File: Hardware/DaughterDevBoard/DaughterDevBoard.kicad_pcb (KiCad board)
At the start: 2 copper layers, 145 x 160 mm, 64 parts, among them J1 PS/2, J10 I/O_PWR, J11 DIVIDER, J12 AUDIO_OUT, J13 BANKA, J14 BANKB, J15 BANKD, J16 BANKC, J17 VGA_OUT, J18 SD_CARD, J2 I/O0, J3 ISA1, J4 ISA0, J5 I/O1, J6 CPU_CLOCK, J7 JOYPAD1, J9 LCD, U1 74HC590A, U2 ATmega328P-PU, U3 SN74LVC2T45QDCURQ1, U4 SN74LVC2T45QDCURQ1, U5 SN74LVC2T45QDCURQ1, U6 SN74LVC8T245DBQR, U7 SN74LVC8T245DBQR, U8 SN74LVC8T245DBQR, X1 ACO-20MHz

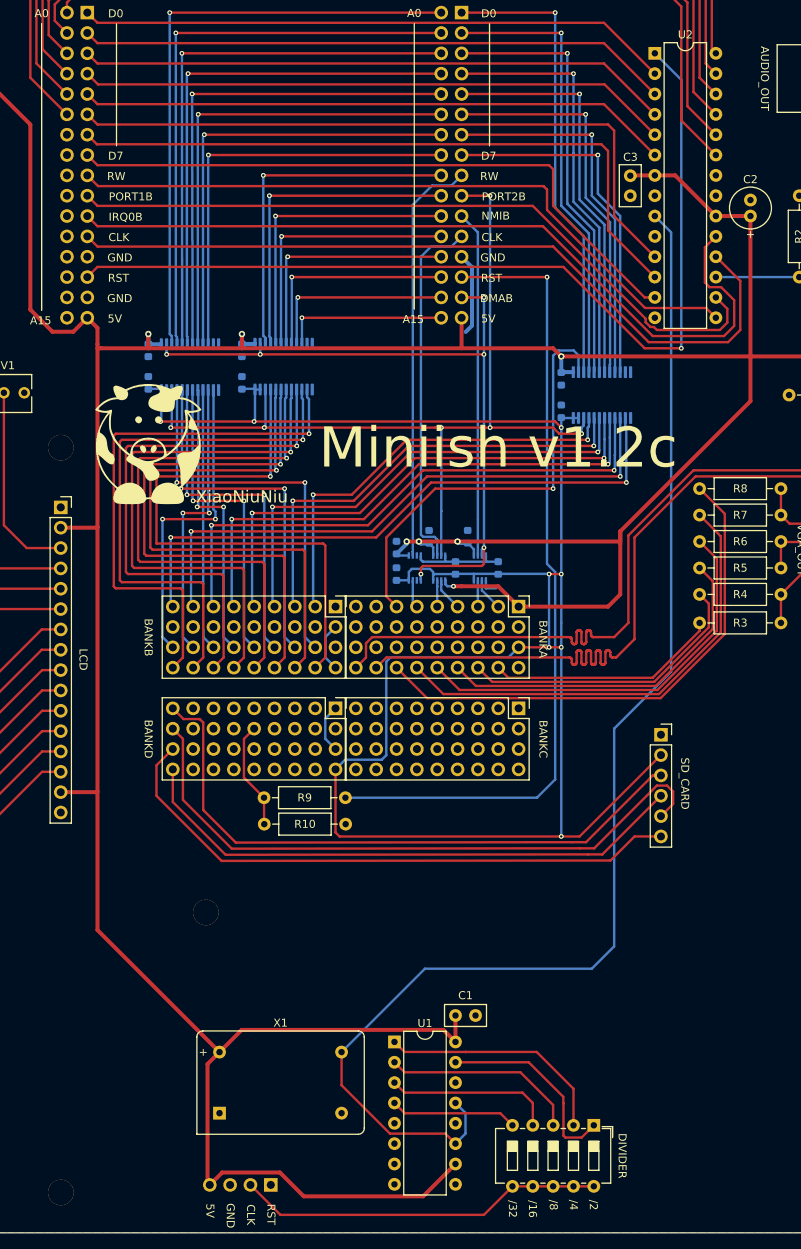
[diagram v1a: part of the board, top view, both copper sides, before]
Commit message: Fix Reset, WAI Signal, Add PROG jumper and reformat luc files
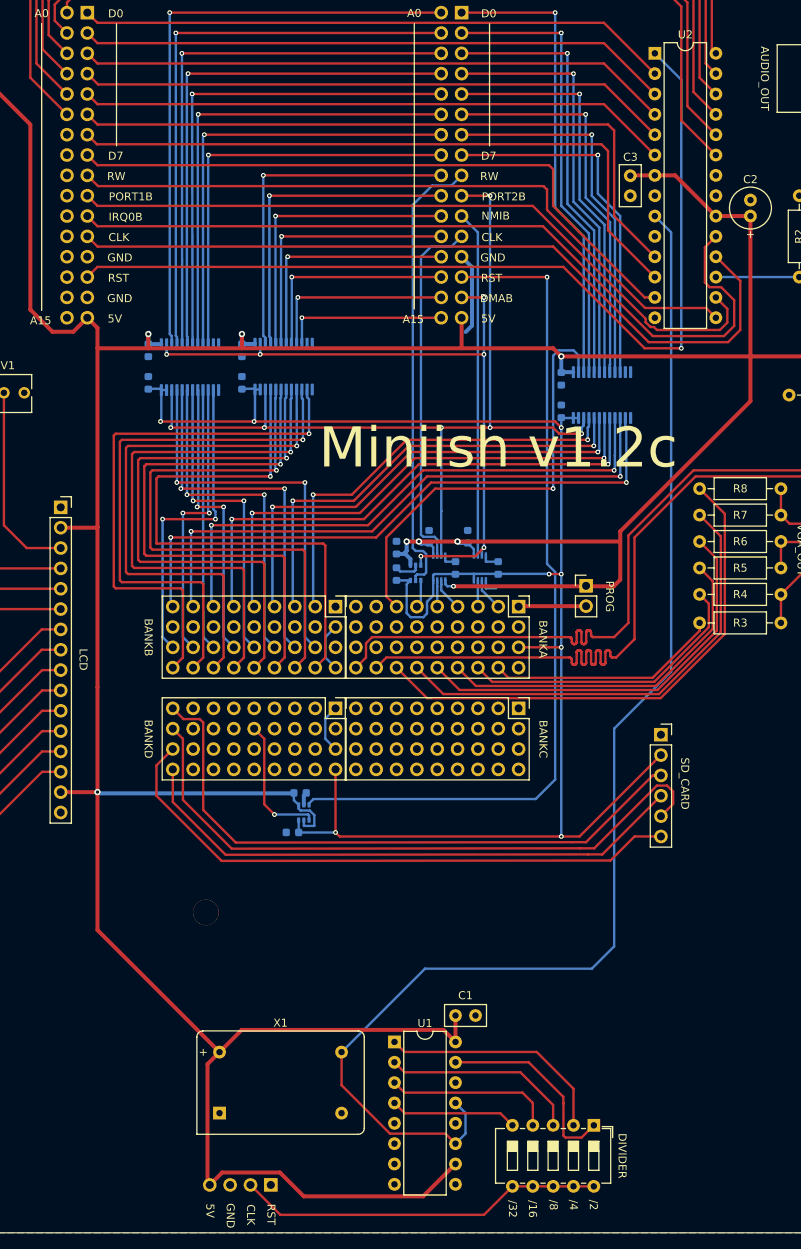
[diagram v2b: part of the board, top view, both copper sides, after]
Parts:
- removed R10: 3K3, Resistor_THT:R_Axial_DIN0207_L6.3mm_D2.5mm_P10.16mm_Horizontal
- removed R9: 2K2, Resistor_THT:R_Axial_DIN0207_L6.3mm_D2.5mm_P10.16mm_Horizontal
- removed REF** (x2): MountingHole_3.2mm_M3, MountingHole:MountingHole_3.2mm_M3
- removed XiaoNiuNiu: LOGO, Logos:SmallCow
- added C18: 100nF, Capacitor_SMD:C_0603_1608Metric, B.Cu at (92.4, 130.5)
- added C19: 100nF, Capacitor_SMD:C_0603_1608Metric, B.Cu at (91.4, 135.4)
- added J8: PROG, Connector_PinHeader_2.54mm:PinHeader_1x02_P2.54mm_Vertical, F.Cu at (128.1, 104.6)
- added U9: SN74LVC1T45DCK, Package_TO_SOT_SMD:SOT-363_SC-70-6, B.Cu at (106.8, 103.0)
- R3, R5, R7: value 1K -> 1.5K
- R4, R6, R8: value 470 -> 680
- U5: value SN74LVC2T45QDCURQ1 -> SN74LVC1T45DCK; footprint Package_SO:VSSOP-8_2.3x2mm_P0.5mm -> Package_TO_SOT_SMD:SOT-363_SC-70-6
- moved U5 33.5 mm to (92.8, 132.9)
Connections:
- net /CLOCK1 renamed /VGA Card/CLOCK1
- net /CLOCK1_1 renamed /SoundCard/CLOCK1
- net /CSB renamed /SoundCard/CSB
- net /CSB_1 renamed /VGA Card/CSB
- net /IRQB renamed /SoundCard/IRQB
- net /NMIB renamed /VGA Card/NMIB
- net /RESET renamed /SoundCard/RESET
- net /RW renamed /SoundCard/RW
- J1 pad 2: (no net) -> unconnected-(J1-Pad2)
- J1 pad 6: (no net) -> unconnected-(J1-Pad6)
- J13 pad 1: +5V -> Net-(J13-Pad1)
- J13 pad 11: (no net) -> unconnected-(J13-Pad11)
- J13 pad 12: (no net) -> unconnected-(J13-Pad12)
- J13 pad 13: (no net) -> unconnected-(J13-Pad13)
- J13 pad 14: (no net) -> unconnected-(J13-Pad14)
- J13 pad 15: (no net) -> unconnected-(J13-Pad15)
- J13 pad 16: (no net) -> unconnected-(J13-Pad16)
- J13 pad 17: (no net) -> unconnected-(J13-Pad17)
- J13 pad 18: (no net) -> unconnected-(J13-Pad18)
- J13 pad 19: (no net) -> unconnected-(J13-Pad19)
- J13 pad 20: (no net) -> unconnected-(J13-Pad20)
- J13 pad 21: (no net) -> unconnected-(J13-Pad21)
- J13 pad 22: (no net) -> unconnected-(J13-Pad22)
- J13 pad 23: (no net) -> unconnected-(J13-Pad23)
- J13 pad 24: (no net) -> unconnected-(J13-Pad24)
- J13 pad 25: (no net) -> unconnected-(J13-Pad25)
- J13 pad 26: (no net) -> unconnected-(J13-Pad26)
- J13 pad 8: (no net) -> unconnected-(J13-Pad8)
- J13 pad 9: (no net) -> unconnected-(J13-Pad9)
- J14 pad 1: (no net) -> unconnected-(J14-Pad1)
- J14 pad 11: (no net) -> unconnected-(J14-Pad11)
- J14 pad 12: (no net) -> unconnected-(J14-Pad12)
- J14 pad 13: (no net) -> unconnected-(J14-Pad13)
- J14 pad 14: (no net) -> unconnected-(J14-Pad14)
- J14 pad 15: (no net) -> unconnected-(J14-Pad15)
- J14 pad 16: (no net) -> unconnected-(J14-Pad16)
- J14 pad 17: (no net) -> unconnected-(J14-Pad17)
- J14 pad 18: (no net) -> unconnected-(J14-Pad18)
- J14 pad 27: (no net) -> unconnected-(J14-Pad27)
- J15 pad 10: (no net) -> unconnected-(J15-Pad10)
- J15 pad 11: (no net) -> unconnected-(J15-Pad11)
- J15 pad 12: (no net) -> unconnected-(J15-Pad12)
- J15 pad 13: (no net) -> unconnected-(J15-Pad13)
- J15 pad 15: (no net) -> unconnected-(J15-Pad15)
- J15 pad 16: (no net) -> unconnected-(J15-Pad16)
- J15 pad 17: (no net) -> unconnected-(J15-Pad17)
- J15 pad 2: (no net) -> unconnected-(J15-Pad2)
- J15 pad 20: (no net) -> unconnected-(J15-Pad20)
- J15 pad 21: (no net) -> unconnected-(J15-Pad21)
- J15 pad 22: (no net) -> unconnected-(J15-Pad22)
- J15 pad 23: (no net) -> unconnected-(J15-Pad23)
- J15 pad 24: (no net) -> unconnected-(J15-Pad24)
- J15 pad 25: (no net) -> unconnected-(J15-Pad25)
- J15 pad 26: (no net) -> unconnected-(J15-Pad26)
- J15 pad 29: (no net) -> unconnected-(J15-Pad29)
- J15 pad 3: (no net) -> unconnected-(J15-Pad3)
- J15 pad 30: (no net) -> unconnected-(J15-Pad30)
- J15 pad 31: (no net) -> unconnected-(J15-Pad31)
- J15 pad 32: (no net) -> unconnected-(J15-Pad32)
- J15 pad 33: (no net) -> unconnected-(J15-Pad33)
- J15 pad 34: (no net) -> unconnected-(J15-Pad34)
- J15 pad 35: (no net) -> unconnected-(J15-Pad35)
- J15 pad 4: (no net) -> unconnected-(J15-Pad4)
- J15 pad 5: (no net) -> unconnected-(J15-Pad5)
- J15 pad 6: (no net) -> unconnected-(J15-Pad6)
- J15 pad 7: (no net) -> unconnected-(J15-Pad7)
- J15 pad 8: (no net) -> unconnected-(J15-Pad8)
- J16 pad 10: (no net) -> unconnected-(J16-Pad10)
- J16 pad 11: (no net) -> unconnected-(J16-Pad11)
- J16 pad 12: (no net) -> unconnected-(J16-Pad12)
- J16 pad 13: (no net) -> unconnected-(J16-Pad13)
- J16 pad 14: (no net) -> unconnected-(J16-Pad14)
- J16 pad 15: (no net) -> unconnected-(J16-Pad15)
- J16 pad 16: (no net) -> unconnected-(J16-Pad16)
- J16 pad 17: (no net) -> unconnected-(J16-Pad17)
- J16 pad 18: (no net) -> unconnected-(J16-Pad18)
- J16 pad 19: (no net) -> unconnected-(J16-Pad19)
- J16 pad 2: (no net) -> unconnected-(J16-Pad2)
- J16 pad 20: (no net) -> unconnected-(J16-Pad20)
- J16 pad 21: (no net) -> unconnected-(J16-Pad21)
- J16 pad 22: (no net) -> unconnected-(J16-Pad22)
- J16 pad 23: (no net) -> unconnected-(J16-Pad23)
- J16 pad 24: (no net) -> unconnected-(J16-Pad24)
- J16 pad 25: (no net) -> unconnected-(J16-Pad25)
- J16 pad 26: (no net) -> unconnected-(J16-Pad26)
- J16 pad 28: (no net) -> unconnected-(J16-Pad28)
- J16 pad 29: (no net) -> unconnected-(J16-Pad29)
- J16 pad 3: (no net) -> unconnected-(J16-Pad3)
- J16 pad 30: (no net) -> unconnected-(J16-Pad30)
- J16 pad 31: (no net) -> unconnected-(J16-Pad31)
- J16 pad 32: (no net) -> unconnected-(J16-Pad32)
- J16 pad 33: (no net) -> unconnected-(J16-Pad33)
- J16 pad 34: (no net) -> unconnected-(J16-Pad34)
- J16 pad 35: (no net) -> unconnected-(J16-Pad35)
- J16 pad 36: (no net) -> unconnected-(J16-Pad36)
- J16 pad 4: (no net) -> unconnected-(J16-Pad4)
- J16 pad 5: (no net) -> unconnected-(J16-Pad5)
- J16 pad 6: (no net) -> unconnected-(J16-Pad6)
- J16 pad 7: (no net) -> unconnected-(J16-Pad7)
- J16 pad 8: (no net) -> unconnected-(J16-Pad8)
- J16 pad 9: (no net) -> unconnected-(J16-Pad9)
- J17 pad 11: (no net) -> unconnected-(J17-Pad11)
- J17 pad 12: (no net) -> unconnected-(J17-Pad12)
- J17 pad 15: (no net) -> unconnected-(J17-Pad15)
- J17 pad 4: (no net) -> unconnected-(J17-Pad4)
- J17 pad 9: (no net) -> unconnected-(J17-Pad9)
- J2 pad 10: (no net) -> CA2
- J2 pad 9: (no net) -> CA1
- J3 pad 14: /RESET_1 -> /VGA Card/RESET
- J3 pad 15: /DMAB -> /VGA Card/DMAB
- J3 pad 9: /RW_1 -> /VGA Card/RW
- J4 pad 23: (no net) -> /AA6
- J4 pad 24: (no net) -> /AA7
- J4 pad 25: (no net) -> /AA8
- J4 pad 26: (no net) -> /AA9
- J4 pad 27: (no net) -> /AA10
- J4 pad 28: (no net) -> /AA11
- J4 pad 29: (no net) -> /AA12
- J4 pad 30: (no net) -> /AA13
- J4 pad 31: (no net) -> /AA14
- J4 pad 32: (no net) -> /AA15
- J5 pad 10: (no net) -> CB2
- J5 pad 9: (no net) -> CB1
- J6 pad 1: (no net) -> RESET
- J7 pad 5: (no net) -> unconnected-(J7-Pad5)
- J7 pad 6: (no net) -> unconnected-(J7-Pad6)
- RV1 pad 3: (no net) -> unconnected-(RV1-Pad3)
- U1 pad 5: (no net) -> unconnected-(U1-Pad5)
- U1 pad 6: (no net) -> unconnected-(U1-Pad6)
- U1 pad 7: (no net) -> unconnected-(U1-Pad7)
- U1 pad 9: (no net) -> unconnected-(U1-Pad9)
- U2 pad 10: (no net) -> unconnected-(U2-Pad10)
- U2 pad 14: (no net) -> unconnected-(U2-Pad14)
- U3 pad 3: /DMAB -> /VGA Card/DMAB
- U5 pad 2: /RW_1 -> GND
- U5 pad 3: (no net) -> /VGA Card/RESET
- U5 pad 4: GND -> Net-(J15-Pad14)
- U5 pad 5: /DMAB -> +5V
- U5 pad 6: (no net) -> +3V3
- U7 pad 2: /DMAB -> /VGA Card/DMAB
- U8 pad 2: /DMAB -> /VGA Card/DMAB
- X1 pad 1: (no net) -> unconnected-(X1-Pad1)
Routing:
- net /VGA Card/RESET: track 0.00 -> 106.0 mm, vias 0 -> 1
- net /RESET_1: track 101.0 -> 0.00 mm, vias 1 -> 0
- net /DMAB: track 89.0 -> 0.00 mm, vias 6 -> 0
- net /VGA Card/DMAB: track 0.00 -> 86.8 mm, vias 0 -> 6
- net /VGA Card/RW: track 0.00 -> 56.8 mm
- net /RW_1: track 51.4 -> 0.00 mm
- net +3V3: track 244.5 -> 212.3 mm
- net +5V: track 565.7 -> 594.3 mm, vias 7 -> 8
- net Net-(J13-Pad1): track 0.00 -> 8.53 mm
- net Net-(J15-Pad14): track 13.5 -> 16.7 mm, vias 0 -> 1
- net GND: track 43.9 -> 41.3 mm

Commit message: Cleanup and update version
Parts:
- added XiaoNiuNiu: LOGO, Logos:SmallCow, F.Cu at (42.0, 175.5)
- moved C18 2.87 mm to (89.9, 131.9), turned to 180 degrees
- moved C19 2.16 mm to (89.9, 133.9)
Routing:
- net +3V3: track 212.3 -> 213.4 mm
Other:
- board text added: "Miniish v1.2d"
- board text removed: "Miniish v1.2c"

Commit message: Cleanup
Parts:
- added C20: 100uF, Capacitor_THT:CP_Radial_D5.0mm_P2.50mm, F.Cu at (109.6, 146.9)
- added Q1: 2N2222A, Package_TO_SOT_THT:TO-18-3, F.Cu at (126.1, 157.7)
- added R10: 1K, Resistor_THT:R_Axial_DIN0207_L6.3mm_D2.5mm_P10.16mm_Horizontal, F.Cu at (114.7, 151.9)
- added R11: 10K, Resistor_THT:R_Axial_DIN0207_L6.3mm_D2.5mm_P10.16mm_Horizontal, F.Cu at (114.8, 144.3)
- added R9: 2.2K, Resistor_THT:R_Axial_DIN0207_L6.3mm_D2.5mm_P10.16mm_Horizontal, F.Cu at (114.8, 148.2)
- C18: value 100nF -> 100uF; footprint Capacitor_SMD:C_0603_1608Metric -> Capacitor_THT:CP_Radial_D5.0mm_P2.50mm; moved to F.Cu
- C19: value 100nF -> 10nF; footprint Capacitor_SMD:C_0603_1608Metric -> Capacitor_THT:C_Disc_D5.0mm_W2.5mm_P2.50mm; moved to F.Cu
- U5: value SN74LVC1T45DCK -> NE555P; footprint Package_TO_SOT_SMD:SOT-363_SC-70-6 -> Package_DIP:DIP-8_W7.62mm; moved to F.Cu
- moved J18 28.9 mm to (166.3, 123.0)
- moved C19 24.1 mm to (106.2, 151.6), turned to -90 degrees
- moved C18 14.7 mm to (91.0, 146.5), turned to 90 degrees
- moved U5 11.4 mm to (95.7, 144.0), turned to 0 degrees
- moved J8 11.0 mm to (136.8, 97.9)
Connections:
- C18 pad 1: +5V -> /VGA Card/RESET
- C19 pad 1: +3V3 -> Net-(C19-Pad1)
- U5 pad 1: +5V -> GND
- U5 pad 2: GND -> /VGA Card/RESET
- U5 pad 3: /VGA Card/RESET -> Net-(R10-Pad1)
- U5 pad 4: Net-(J15-Pad14) -> +5V
- U5 pad 5: +5V -> Net-(C19-Pad1)
- U5 pad 6: +3V3 -> Net-(C20-Pad1)
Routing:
- net Net-(J15-Pad14): track 17.2 -> 57.4 mm, vias 1 -> 0
- net MISO: track 74.3 -> 100.0 mm
- net SCK: track 80.4 -> 103.1 mm
- net MOSI: track 70.8 -> 93.3 mm
- net SS: track 77.7 -> 100.0 mm
- net +3V3: track 213.4 -> 235.6 mm, vias 8 -> 7
- net Net-(R10-Pad1): track 0.00 -> 20.2 mm
- net /VGA Card/RESET: track 105.9 -> 124.3 mm
- net +5V: track 594.2 -> 609.0 mm, vias 8 -> 7
- net Net-(C20-Pad1): track 0.00 -> 14.7 mm
- net Net-(J13-Pad1): track 8.53 -> 20.0 mm
- net APU_CLOCK: track 162.0 -> 168.9 mm
- net Net-(Q1-Pad2): track 0.00 -> 4.52 mm
- net Net-(C19-Pad1): track 0.00 -> 2.91 mm
- net GND: track 40.9 -> 39.7 mm
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
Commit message: Fix
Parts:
- added J19: BANK_A, 4UCON:4UCON_2x25_P0.50mm_Vertical, F.Cu at (245.9, 112.7)
- added J20: BANK_C, 4UCON:4UCON_2x25_P0.50mm_Vertical, F.Cu at (220.4, 112.7)
- added J21: BANK_B, 4UCON:4UCON_2x25_P0.50mm_Vertical, F.Cu at (241.9, 148.7)
- added J22: BANK_D, 4UCON:4UCON_2x25_P0.50mm_Vertical, F.Cu at (220.4, 148.7)
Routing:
- net unconnected-(J14-Pad18): vias 0 -> 3
- net unconnected-(J14-Pad17): vias 0 -> 3
- net unconnected-(J14-Pad16): vias 0 -> 3
- net unconnected-(J14-Pad15): vias 0 -> 3
- net unconnected-(J14-Pad14): vias 0 -> 3
- net unconnected-(J13-Pad9): vias 0 -> 1
- net unconnected-(J13-Pad18): vias 0 -> 1
- net unconnected-(J13-Pad17): vias 0 -> 3
- net unconnected-(J13-Pad16): vias 0 -> 3
- net unconnected-(J13-Pad15): vias 0 -> 3
- net unconnected-(J13-Pad14): vias 0 -> 3
- net unconnected-(J13-Pad13): vias 0 -> 3
- net Net-(J15-Pad14): vias 0 -> 6
- net Net-(J14-Pad9): vias 2 -> 3
- net Net-(J14-Pad8): vias 2 -> 3
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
